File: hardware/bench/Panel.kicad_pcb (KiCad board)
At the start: 4 copper layers, 151 x 139 mm, 390 parts

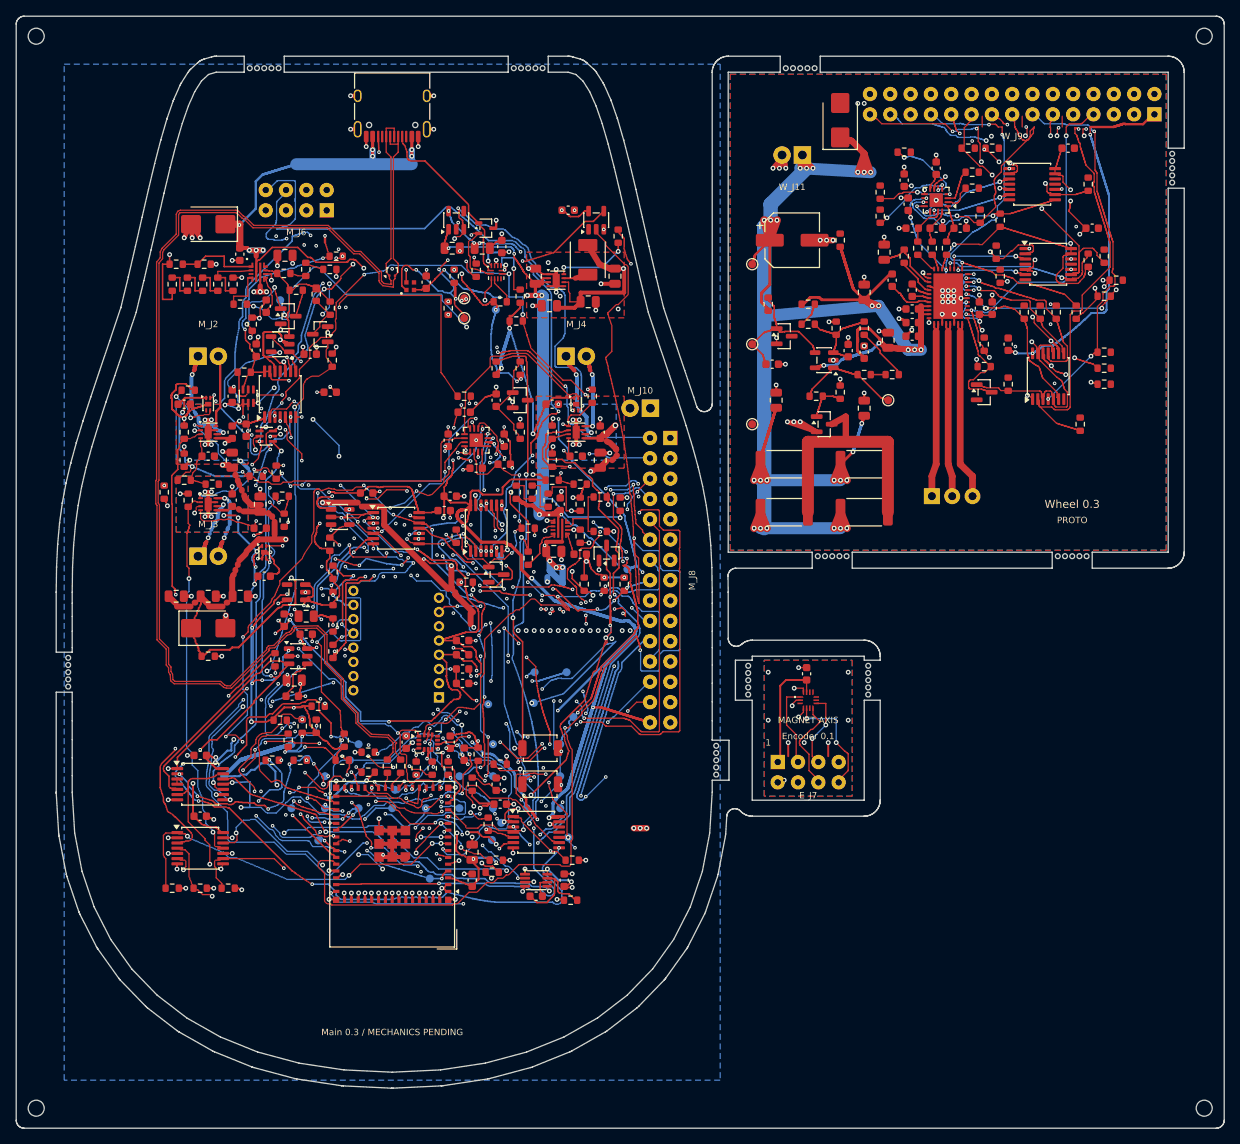
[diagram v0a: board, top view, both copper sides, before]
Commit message: Repair copper contacts and make manufacturing panel router-compatible
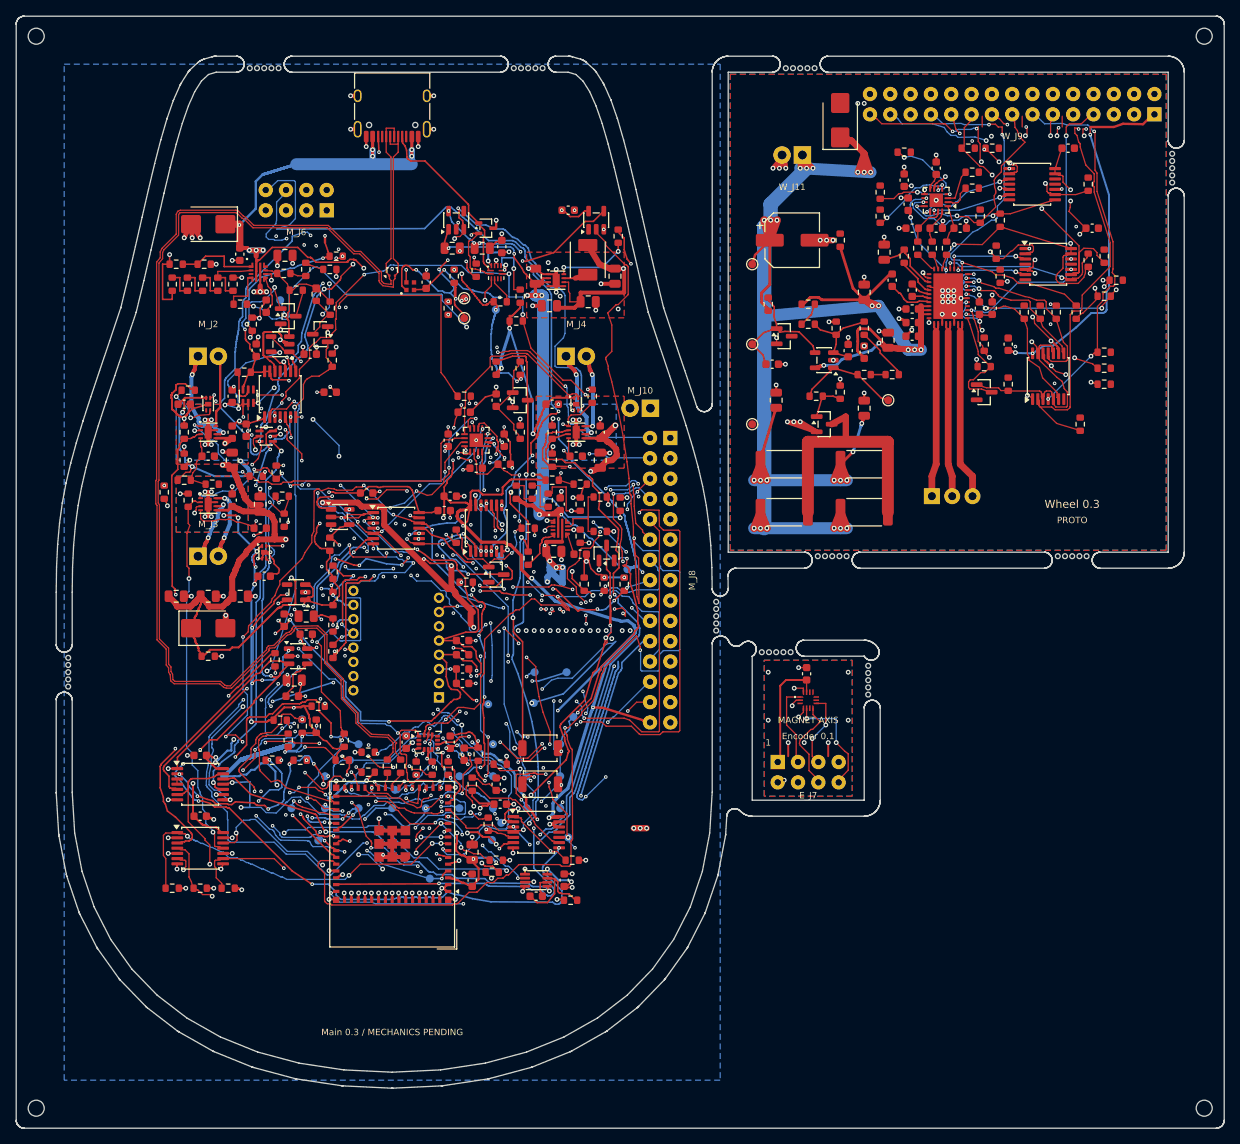
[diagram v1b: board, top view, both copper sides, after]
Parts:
- moved MB4_1 18.0 mm to (87.5, 73.2)
- moved MB4_2 18.0 mm to (87.5, 74.1)
- moved MB4_3 18.0 mm to (87.5, 75.0)
- moved MB4_4 18.0 mm to (87.5, 75.9)
- moved MB4_5 18.0 mm to (87.5, 76.8)
- moved MB9_1 5.57 mm to (93.2, 79.5)
- moved MB9_5 5.57 mm to (96.8, 79.5)
- moved MB9_2 5.11 mm to (94.1, 79.5)
- moved MB9_4 5.11 mm to (95.9, 79.5)
- moved MB9_3 4.95 mm to (95.0, 79.5)
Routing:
- net Main/ACT_5V: track 200.7 -> 360.5 mm
- net Main/+3V3: track 589.9 -> 629.5 mm
- net Main/VBUS_USB: track 148.2 -> 182.2 mm
- net Main/HALL_EN: track 211.9 -> 241.7 mm
- net Main/BTN_R_IN2: track 52.3 -> 73.3 mm
- net Main/MCU_EN: track 179.4 -> 198.0 mm
- net Main/GND: track 269.0 -> 286.6 mm
- net Main/CC_OUT2: track 114.0 -> 130.8 mm
- net Main/WHEEL_PWM_B: track 137.0 -> 153.2 mm
- net Main/SPI_MOSI: track 192.6 -> 208.7 mm
- net Main/OPT_CTRL: track 105.0 -> 121.0 mm
- net Main/BTN_R_IN1: track 52.1 -> 67.9 mm
- net Main/ACT_DRIVE_EN: track 120.6 -> 136.2 mm
- net Main/CS_PAW: track 91.3 -> 106.7 mm
- net Main/WHEEL_PWM_C: track 43.7 -> 57.7 mm
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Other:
- outline, holes or cut-outs redrawn
